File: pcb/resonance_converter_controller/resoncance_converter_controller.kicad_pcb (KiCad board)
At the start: 6 copper layers, 61.4 x 82.1 mm, 259 parts, among them J1 Micro_SD_Card_Det2, J2 USB_C_Receptacle_USB2.0_14P, J4 Conn_02x19_Odd_Even, J5 Conn_01x02, J6 FX18-120S-0.8SH, J7 Conn_ARM_SWD_TagConnect_TC2030, Q1 FDMC8032L, Q2 FDMC8032L, Q3 SiR696DP, SW1 SW_SPST, SW2 SW_SPST, U1 BQ25792RQMR, U10 INA280A1xDCK, U11 INA280A1xDCK, U12 INA280A1xDCK, U13 STM32G474VEHx, U14 APS6404L-SQRx-ZR, U15 APS6404L-SQRx-ZR, U16 AT24CS32-XHM, U17 TL3116, U18 OPA2356xxDGK, U19 TMUX154ERSW, U2 TPS55289RYQR, U20 OPA356xxDBV, U21 TPS2553DRVR, U22 USBLC6-2P6, U23 OPA356xxDBV, U24 AD5246BKSZ100-RL7, U3 TPS54240DRC, U4 TPS73733DCQR, U5 OPA2325, U6 LP5907MFX-3.3, U7 OPA2356xxDGK, U8 OPA356xxDBV, U9 INA280A1xDCK, Y1 16Mhz

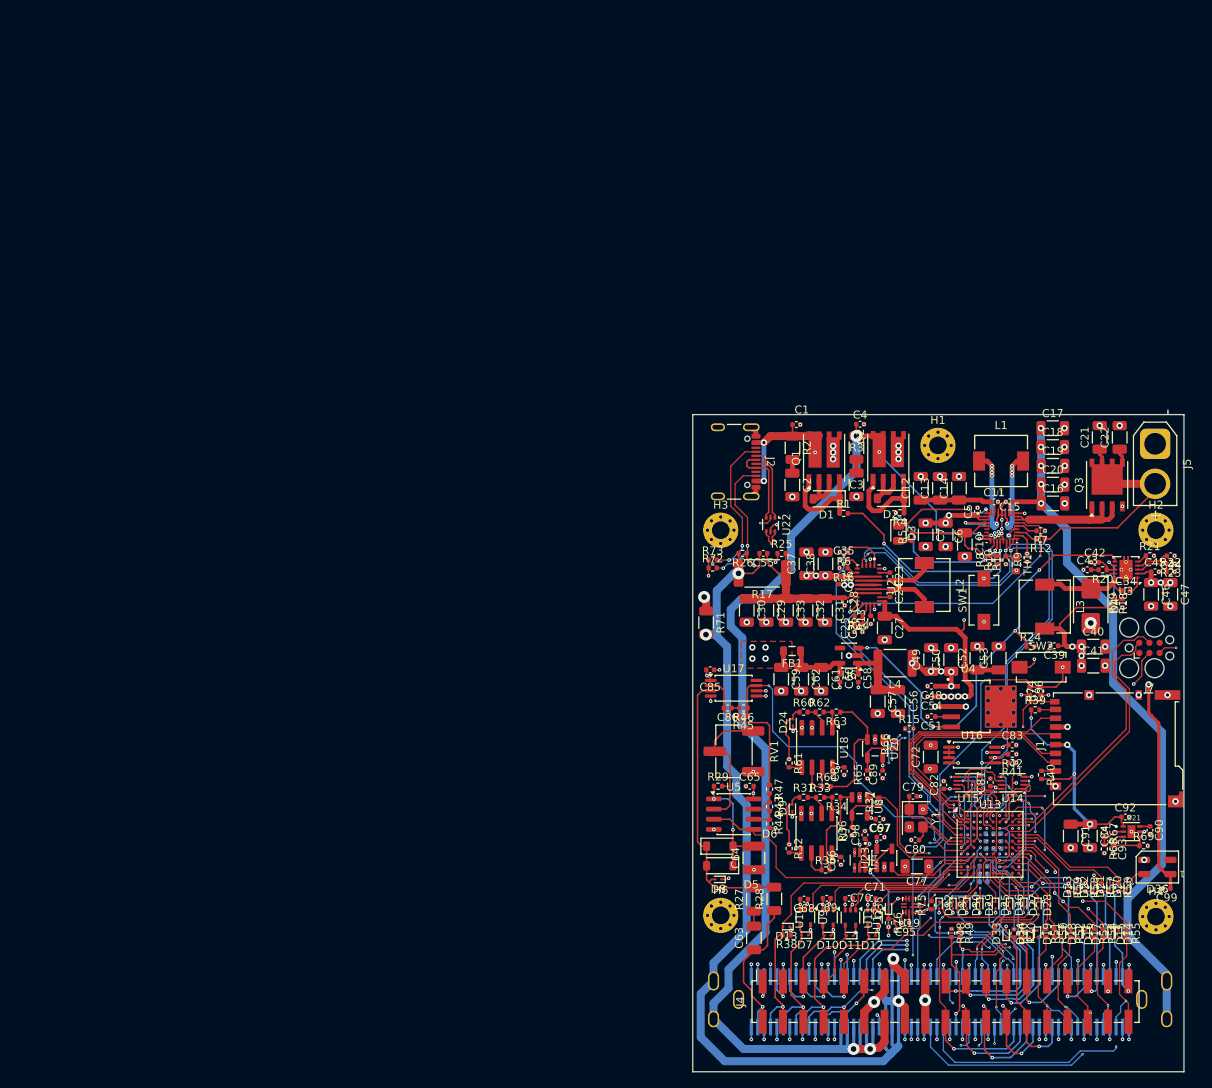
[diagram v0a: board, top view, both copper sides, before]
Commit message: Add io panel and fix controller pcb
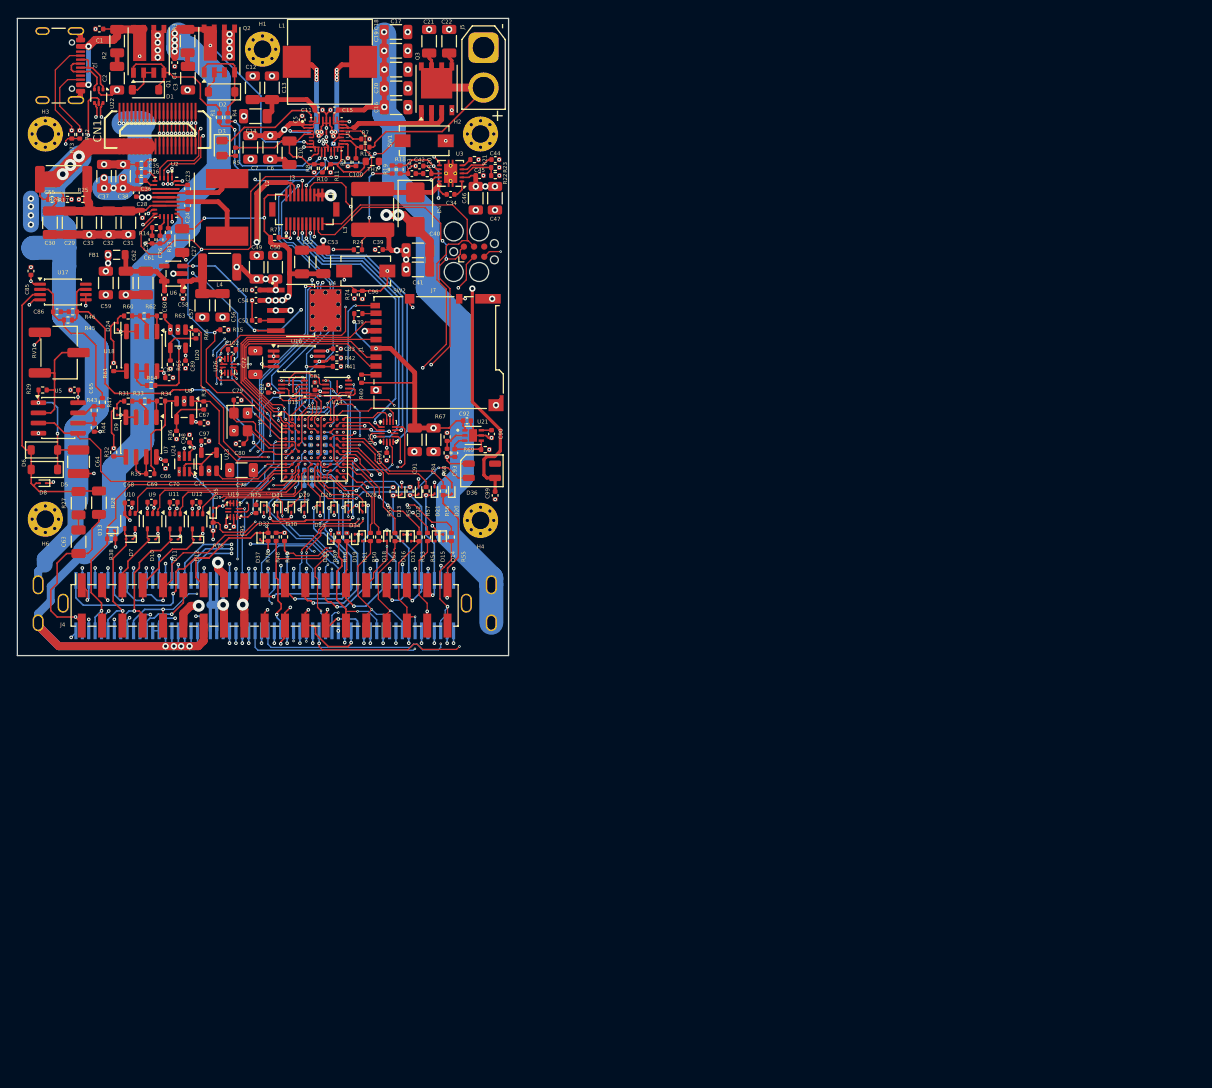
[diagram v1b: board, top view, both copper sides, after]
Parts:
- added C100: 47nF, Capacitor_SMD:C_0402_1005Metric, F.Cu at (128.6, 54.9)
- added C101: 100nF, Capacitor_SMD:C_0402_1005Metric, F.Cu at (132.4, 91.7)
- added C102: 100nF, Capacitor_SMD:C_0402_1005Metric, F.Cu at (113.0, 78.3)
- added CN1: AXK5S40047YG, AXK5S40047YG:CONN-SMD_40P-P0.50_AXK5S40047YG, F.Cu at (103.8, 50.7)
- added D37: ESD9B3.3ST5G, Diode_SMD:D_SOD-923, F.Cu at (116.6, 101.7)
- added J3: DF12NB_5.0_-20DP-0.5V_51_, DF12NB_5.0_-20DP-0.5V_51_:HRS_DF12NB_5.0_-20DP-0.5V_51_, F.Cu at (122.1, 60.8)
- added R77: 10k, Resistor_SMD:R_0402_1005Metric, F.Cu at (118.4, 64.3)
- added R78: 10K, Resistor_SMD:R_0402_1005Metric, F.Cu at (117.6, 101.7)
- added U25: TMUX1574RSV, Package_DFN_QFN:UQFN-16_1.8x2.6mm_P0.4mm, F.Cu at (132.6, 88.6)
- added U26: TMUX154ERSW, Package_DFN_QFN:UQFN-10_1.4x1.8mm_P0.4mm, F.Cu at (112.6, 80.3)
- L1: footprint Inductor_SMD:L_6.3x6.3_H3 -> Inductor_SMD:L_10.4x10.4_H4.8
- L2: value 4.7uH -> ASPI-8030LR-4R7M-T; footprint Inductor_SMD:L_6.3x6.3_H3 -> ASPI-8030LR-4R7M-T:IND_ASPI-8030LR-4R7M-T
- L3: footprint Inductor_SMD:L_6.3x6.3_H3 -> Capacitor_SMD:C_2220_5750Metric
- R71: moved to B.Cu
- moved R19 105.3 mm to (134.1, 55.8)
- moved R18 105.3 mm to (133.1, 55.8)
- moved R66 101.3 mm to (108.5, 76.4)
- moved R65 101.1 mm to (105.3, 80.2)
- moved C89 101.1 mm to (107.2, 80.2)
- moved U20 101.1 mm to (106.3, 77.0)
- moved R14 100.3 mm to (103.6, 63.1)
- moved C25 100.3 mm to (103.1, 64.6)
- moved C26 100.3 mm to (104.1, 64.6)
- moved C27 100.3 mm to (106.8, 64.7)
- moved C23 100.3 mm to (107.5, 58.2)
- moved C24 100.3 mm to (107.5, 60.3)
- moved C37 100.3 mm to (97.1, 56.6)
- moved C38 100.3 mm to (99.4, 56.7)
- moved C28 100.3 mm to (101.9, 61.4)
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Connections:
- net /Controller/NRST renamed NRST
- net /Controller/SWCLK renamed SWCLK
- net /Controller/SWDIO renamed SWDIO
- net Net-(SW1-B) renamed /QON
- J4 pad 13: GND -> AUX_ADC
- J6 pad 19: ENCODER_CHB -> REMOTE_ENCODER_CHB
- J6 pad 20: LCD_DC -> REMOTE_LCD_DC
- J6 pad 29: LCD_SCK -> REMOTE_LCD_SCK
- J6 pad 60: GND -> AUX_ADC
- J6 pad 80: ENCODER_CHA -> REMOTE_ENCODER_CHA
- J6 pad 90: LCD_MOSI -> REMOTE_LCD_MOSI
- J6 pad 92: LCD_SS -> REMOTE_LCD_SS
- J6 pad SH1: GND -> (no net)
- U13 pad H10: unconnected-(U13-PD11-PadH10) -> LOCAL_LCD
- U13 pad H4: unconnected-(U13-PB0-PadH4) -> LOCAL_ENCODER
- U13 pad J3: unconnected-(U13-PC5-PadJ3) -> KEY_INT
- U13 pad K1: unconnected-(U13-PA7-PadK1) -> AUX_ADC
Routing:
- net GND: track 179.5 -> 299.6 mm, vias 239 -> 238
- net LCD_MOSI: track 63.7 -> 6.77 mm, vias 2 -> 0
- net REMOTE_LCD_MOSI: track 0.00 -> 56.9 mm, vias 0 -> 2
- net REMOTE_LCD_SS: track 0.00 -> 55.5 mm, vias 0 -> 2
- net LCD_SS: track 61.0 -> 6.12 mm, vias 2 -> 0
- net VSYS: track 106.6 -> 153.5 mm, vias 13 -> 29
- net AUX_ADC: track 0.00 -> 46.7 mm, vias 0 -> 3
- net REMOTE_ENCODER_CHA: track 0.00 -> 45.9 mm, vias 0 -> 5
- net KEY_INT: track 0.00 -> 44.3 mm, vias 0 -> 4
- net LOCAL_ENCODER_CHA: track 0.00 -> 43.1 mm, vias 0 -> 4
- net REMOTE_LCD_SCK: track 0.00 -> 41.7 mm, vias 0 -> 2
- net LCD_SCK: track 47.3 -> 8.46 mm
- net REMOTE_ENCODER_CHB: track 0.00 -> 37.8 mm, vias 0 -> 2
- net LOCAL_LCD_SS: track 0.00 -> 37.6 mm, vias 0 -> 2
- net LOCAL_LCD_SCK: track 0.00 -> 36.1 mm, vias 0 -> 2
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- removed copper zone on F.Cu, net VAA
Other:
- board size 61.4 x 82.1 mm -> 61.4 x 79.7 mm

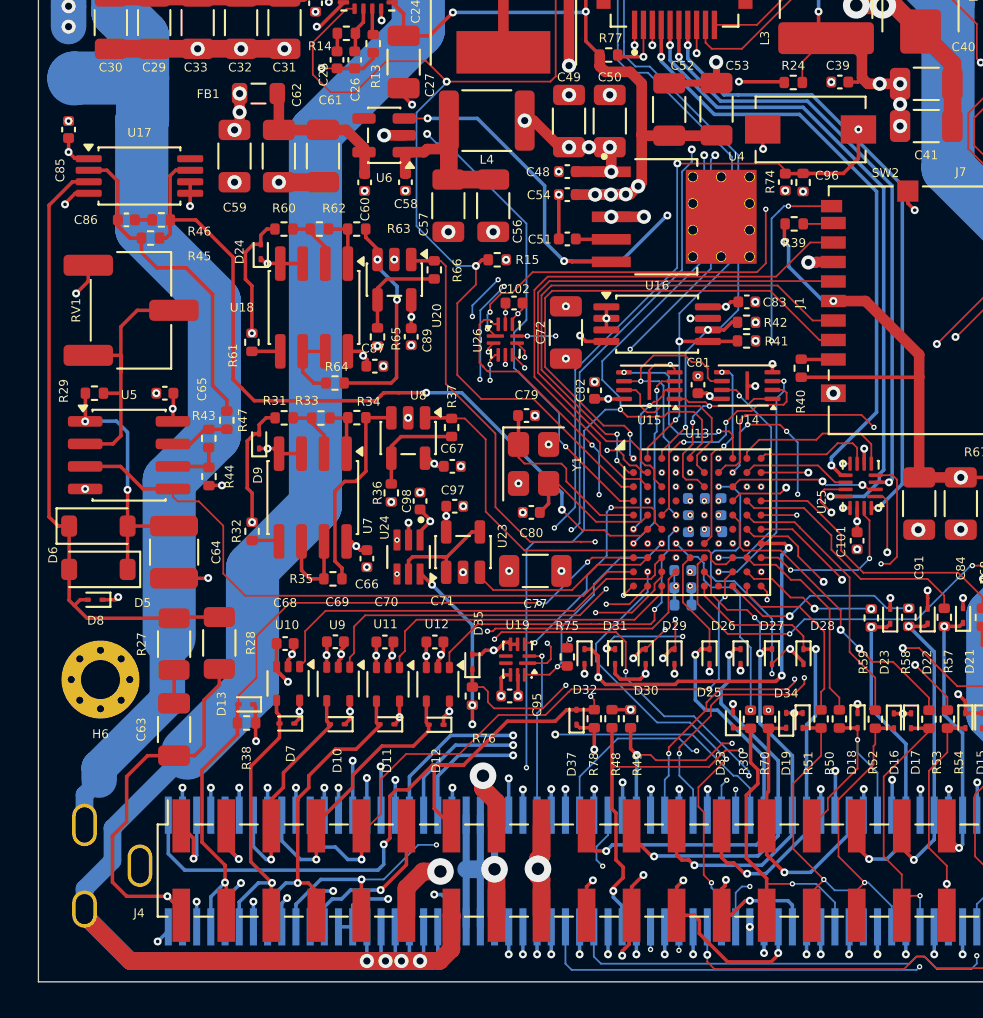
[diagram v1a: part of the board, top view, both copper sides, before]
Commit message: Add digital pots to auto adjust gain
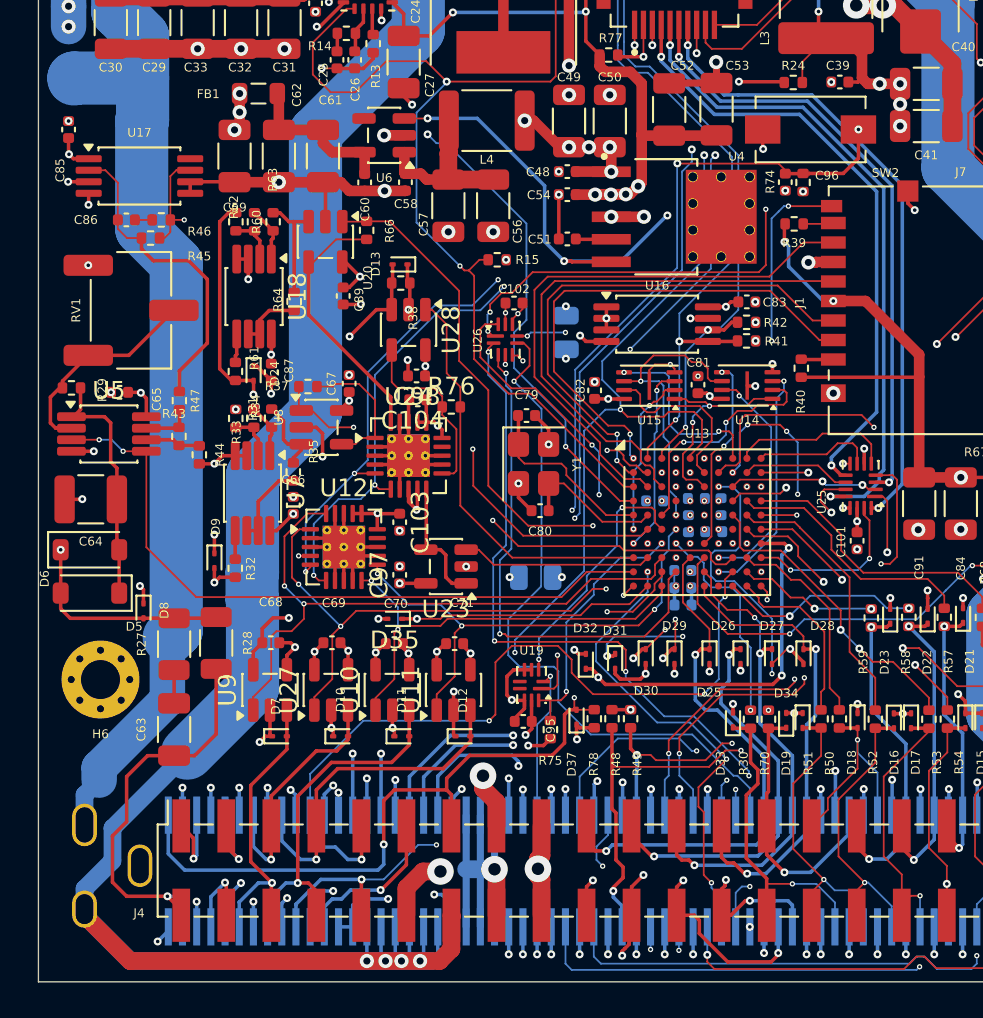
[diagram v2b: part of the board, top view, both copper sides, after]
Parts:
- removed R36, R65: 10K, Resistor_SMD:R_0402_1005Metric
- added C103: 100nF, Capacitor_SMD:C_0402_1005Metric, F.Cu at (106.6, 90.7)
- added C104: 100nF, Capacitor_SMD:C_0402_1005Metric, F.Cu at (107.6, 83.8)
- added C105: 100nF, Capacitor_SMD:C_0402_1005Metric, B.Cu at (121.0, 89.5)
- added U27: INA169, Package_TO_SOT_SMD:SOT-23-5, F.Cu at (102.7, 100.1)
- added U28: OPA356xxDBV, Package_TO_SOT_SMD:SOT-23-5, F.Cu at (107.1, 79.8)
- C72, C77: footprint Capacitor_SMD:C_1206_3216Metric -> Capacitor_SMD:C_0805_2012Metric; moved to B.Cu
- R76: value 5.1K -> 10K
- U10, U11, U9: value INA280A1xDCK -> INA169; footprint Package_TO_SOT_SMD:SOT-353_SC-70-5 -> Package_TO_SOT_SMD:SOT-23-5
- U12: value INA280A1xDCK -> MCP4441-xxxx-ST; footprint Package_TO_SOT_SMD:SOT-353_SC-70-5 -> Package_DFN_QFN:Texas_RGP0020H_VQFN-20-1EP_4x4mm_P0.5mm_EP2.4x2.4mm_ThermalVias
- U18, U5, U7: footprint Package_SO:SOIC-8_3.9x4.9mm_P1.27mm -> Package_SO:VSSOP-8_3x3mm_P0.65mm
- U24: value AD5246BKSZ100-RL7 -> MCP4441-xxxx-ST; footprint AD5246BKSZ100-RL7:SOT65P210X110-6N -> Package_DFN_QFN:Texas_RGP0020H_VQFN-20-1EP_4x4mm_P0.5mm_EP2.4x2.4mm_ThermalVias
- moved R38 26.3 mm to (106.7, 77.2)
- moved D13 26.3 mm to (106.6, 76.1)
- moved R76 16.4 mm to (109.5, 84.2), turned to 0 degrees
- moved U12 9.39 mm to (103.5, 92.0), turned to 0 degrees
- moved R37 8.43 mm to (101.4, 83.0), turned to 180 degrees
- moved C67 7.46 mm to (103.8, 82.8), turned to -90 degrees
- moved D9 7.20 mm to (96.2, 92.8), turned to -90 degrees
- moved C98 7.06 mm to (107.5, 82.4), turned to 180 degrees
- moved D24 6.87 mm to (98.4, 82.3), turned to -90 degrees
- moved R35 6.44 mm to (100.6, 87.8), turned to 90 degrees
- moved C87 5.85 mm to (99.4, 82.2), turned to 90 degrees
- moved U24 5.71 mm to (107.1, 86.9), turned to 0 degrees
- moved C64 5.57 mm to (89.2, 89.4), turned to 0 degrees
- moved R64 5.15 mm to (100.7, 78.2), turned to 90 degrees
- moved C66 5.12 mm to (100.6, 89.7), turned to -90 degrees
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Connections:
- net /Controller/DAC_CH1 renamed /Analog preprocess/DAC_IN
- D35 pad 1: /Controller/DAC_READ_BACK -> DAC_OUT
- R37 pad 1: Net-(U8--) -> Net-(U24D-P3A)
- R76 pad 1: /Controller/DAC_READ_BACK -> Net-(U24A-P0A)
- R76 pad 2: DAC_OUT -> /Analog preprocess/VSENSE_OUT
- U10 pad 1: /Analog preprocess/ISENSE_2_OUT -> /Analog preprocess/ISENSE_3_OUT
- U10 pad 3: VAA -> ISENSE_3
- U10 pad 4: ISENSE_2 -> GND
- U10 pad 5: GND -> VAA
- U11 pad 1: /Analog preprocess/ISENSE_3_OUT -> /Analog preprocess/ISENSE_4_OUT
- U11 pad 3: VAA -> ISENSE_4
- U11 pad 4: ISENSE_3 -> GND
- U11 pad 5: GND -> VAA
- U12 pad 1: /Analog preprocess/ISENSE_4_OUT -> /Analog preprocess/ISENSE_2_OUT
- U12 pad 3: VAA -> GND
- U12 pad 4: ISENSE_4 -> VCC
- U12 pad 5: GND -> INT_I2C_SCL
- U13 pad D3: unconnected-(U13-VBAT-PadD3) -> VCC
- U13 pad H1: VSENSE_IN -> /Analog preprocess/VSENSE_OUT
- U13 pad K2: /Controller/DAC_READ_BACK -> DAC_OUT
- U24 pad 1: VAA -> Net-(U24D-P3A)
- U24 pad 3: INT_I2C_SCL -> GND
- U24 pad 4: INT_I2C_SDA -> GND
- U24 pad 5: Net-(U23--) -> INT_I2C_SCL
- U24 pad 6: DAC_OUT -> INT_I2C_SDA
- U8 pad 4: Net-(U8--) -> Net-(U24D-P3A)
- U9 pad 3: VAA -> ISENSE_1
- U9 pad 4: ISENSE_1 -> GND
- U9 pad 5: GND -> VAA
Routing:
- net GND: track 299.6 -> 355.5 mm, vias 238 -> 230
- net /Analog preprocess/VSENSE_OUT: track 0.00 -> 23.1 mm
- net DAC_OUT: track 30.3 -> 48.5 mm, vias 4 -> 3
- net /Controller/DAC_READ_BACK: track 15.9 -> 0.00 mm, vias 2 -> 0
- net VCC: track 101.9 -> 117.0 mm, vias 29 -> 33
- net /Analog preprocess/ISENSE_1_OUT: track 24.3 -> 36.5 mm, vias 0 -> 2
- net /Analog preprocess/ISENSE_2_OUT: track 25.1 -> 36.1 mm, vias 2 -> 4
- net Net-(U24A-P0A): track 0.00 -> 10.4 mm
- net /Analog preprocess/ISENSE_4_OUT: track 18.8 -> 28.1 mm, vias 2 -> 4
- net Net-(U20--): track 5.65 -> 14.8 mm
- net Net-(U24D-P3A): track 0.00 -> 8.04 mm
- net HRTIM_FLT3: track 37.7 -> 45.4 mm, vias 3 -> 4
- net Net-(U8-+): track 11.8 -> 4.35 mm
- net /Analog preprocess/ISENSE_3_OUT: track 17.9 -> 25.1 mm, vias 0 -> 2
- net /Analog preprocess/FB_OCD_RECTIFIED: track 23.5 -> 30.5 mm, vias 0 -> 2
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
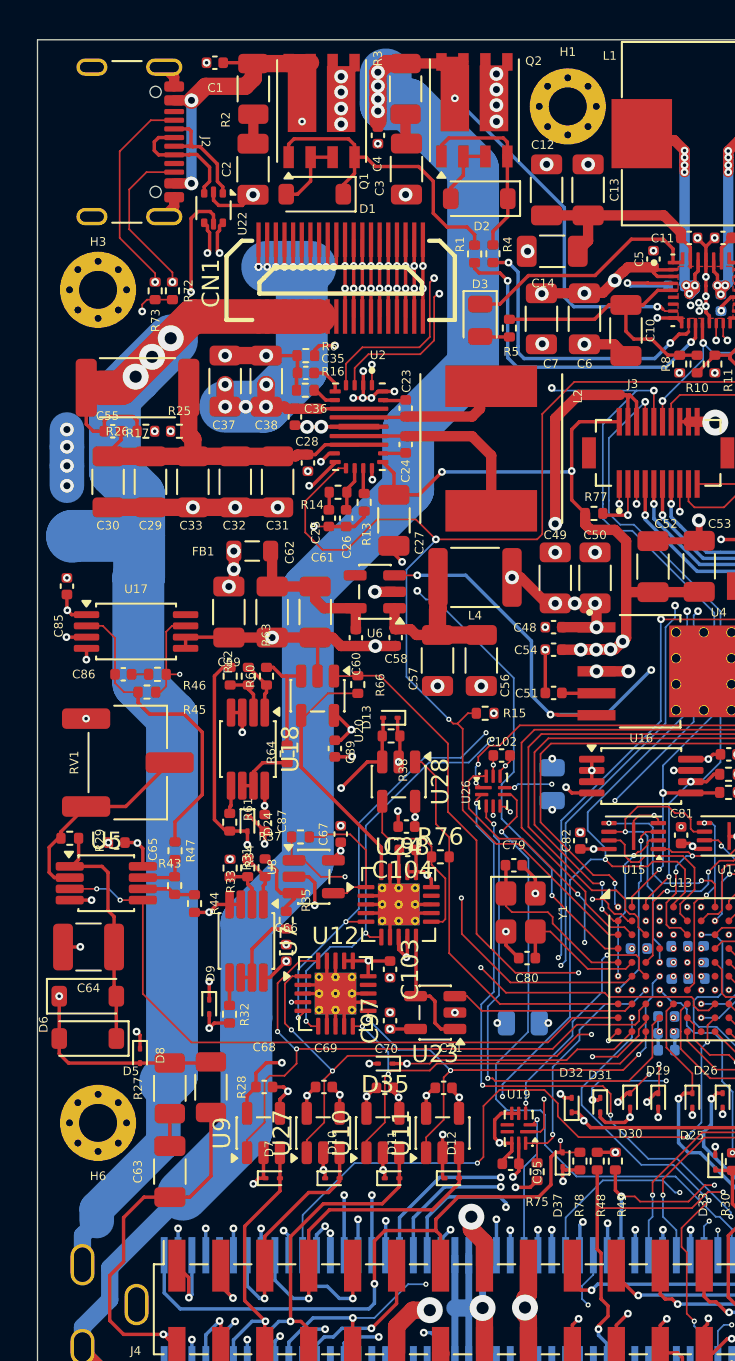
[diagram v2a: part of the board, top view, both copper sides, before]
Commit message: Reroute USB fix silkscreen and Kicad 9 -> 10
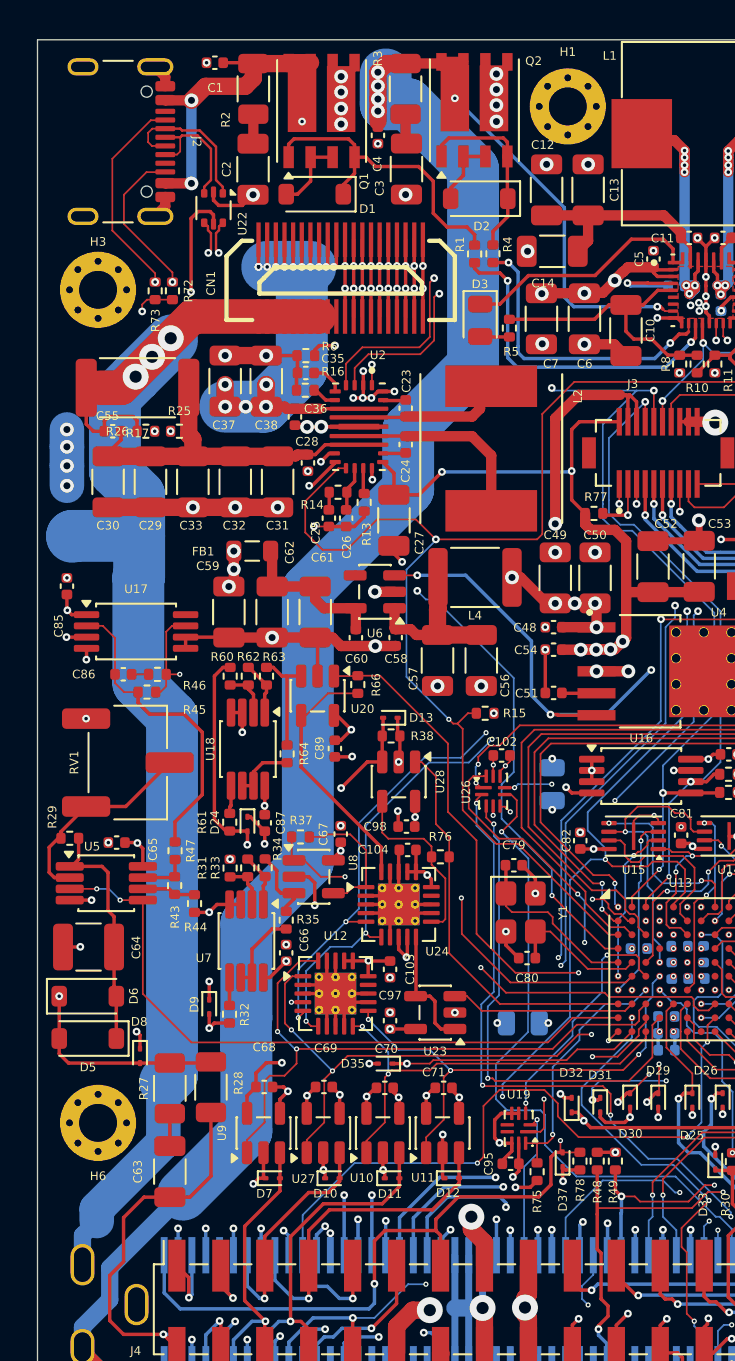
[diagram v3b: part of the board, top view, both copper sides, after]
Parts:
- moved J2 0.52 mm to (89.9, 42.8)
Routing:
- net /PUSB-: track 6.72 -> 8.93 mm
- net VBUS_USBC: track 46.8 -> 47.8 mm
- net GND: track 355.5 -> 356.0 mm
